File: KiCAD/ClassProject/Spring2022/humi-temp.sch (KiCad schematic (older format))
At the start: 2 parts

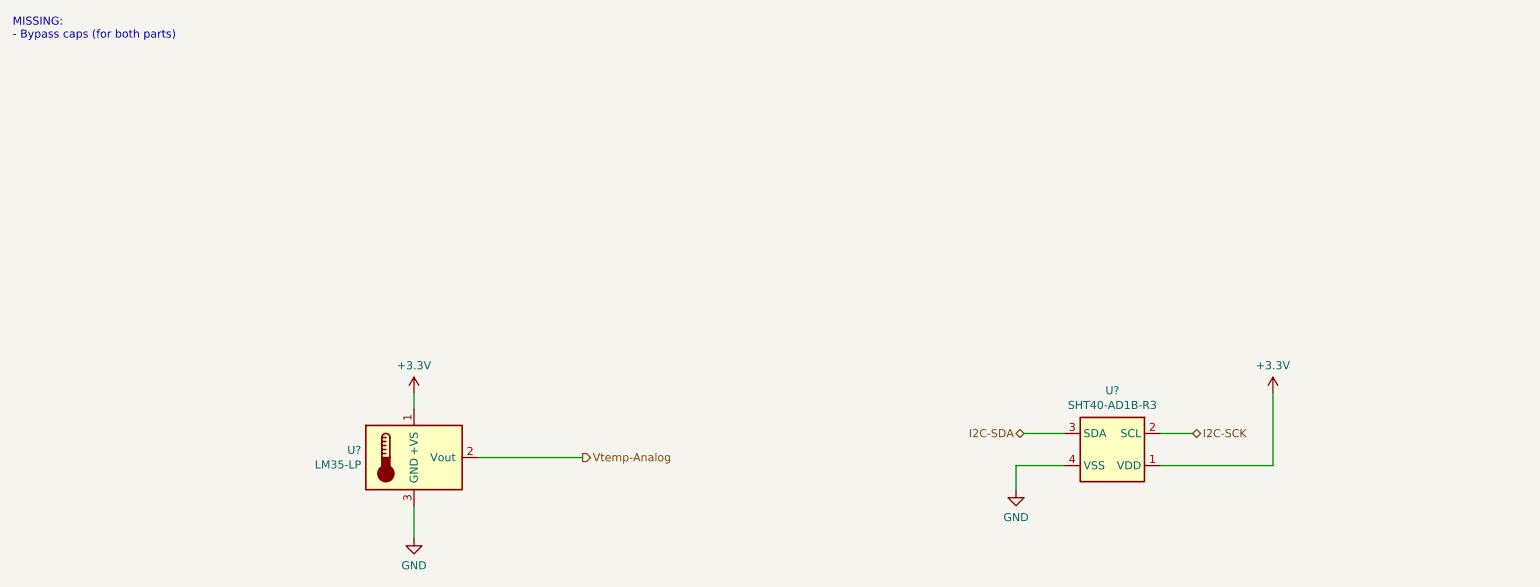
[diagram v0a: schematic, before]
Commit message: Added decoupling caps and pull up resistors from PONTECH library
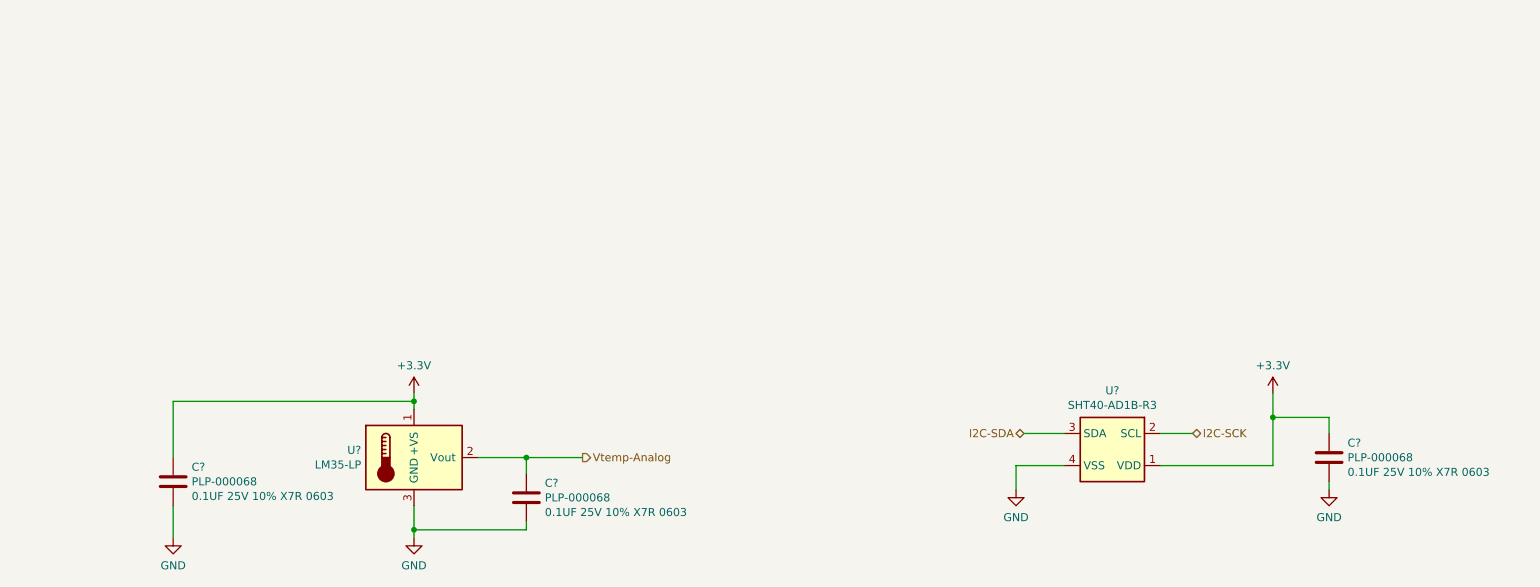
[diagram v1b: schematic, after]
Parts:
- added C? (x3): PLP-000068, a_pontech:CAP-NON-POLAR-0603, symbol 1_pontech:PLP-000068
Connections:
- net +3V3: now also C?.1, C?.1
- net GND: now also C?.2, C?.2, C?.2
- net Vtemp-Analog: now also C?.1
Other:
- note removed: "MISSING:\n- Bypass caps (for both parts)"
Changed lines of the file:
@@
 Comment4 ""
 $EndDescr
-Text Notes 950  1000 0    50   ~ 0
-MISSING:\n- Bypass caps (for both parts)
 $Comp
 L 74_Jacob:+3.3V #PWR?
@@
 $EndComp
 Wire Wire Line
-	8800 3200 8800 3650
+	8800 3200 8800 3350
 Wire Wire Line
 	8800 3650 8100 3650
@@
 $EndComp
 Wire Wire Line
-	3450 4100 3450 3900
+	3450 4100 3450 4050
 Text HLabel 4500 3600 2    50   Output ~ 0
 Vtemp-Analog
 Wire Wire Line
-	3850 3600 4500 3600
+	3850 3600 4150 3600
 $Comp
 L 74_Jacob:+3.3V #PWR?
@@
 	1    0    0    -1
 $EndComp
-Wire Wire Line
-	3450 3200 3450 3300
 Text HLabel 7250 3450 0    50   BiDi ~ 0
 I2C-SDA
@@
 Wire Wire Line
 	8300 3450 8100 3450
+$Comp
+L 1_pontech:PLP-000068 C?
+U 1 1 6264748D
+P 4150 3850
+F 0 "C?" H 4265 3941 50  0000 L CNN
+F 1 "PLP-000068" H 4265 3850 50  0000 L CNN
+F 2 "a_pontech:CAP-NON-POLAR-0603" H 4250 3400 50  0001 L CNN
+F 3 "~" H 4150 3850 50  0001 C CNN
+F 4 "0.1UF 25V 10% X7R 0603" H 4265 3759 50  0000 L CNN "Info"
+	1    4150 3850
+	1    0    0    -1
+$EndComp
+Connection ~ 4150 3600
+Wire Wire Line
+	4150 3600 4500 3600
+Wire Wire Line
+	4150 4050 3450 4050
+Connection ~ 3450 4050
+Wire Wire Line
+	4150 3700 4150 3600
+Wire Wire Line
+	4150 4000 4150 4050
+$Comp
+L 1_pontech:PLP-000068 C?
+U 1 1 626498A3
+P 1950 3750
+F 0 "C?" H 2065 3841 50  0000 L CNN
+F 1 "PLP-000068" H 2065 3750 50  0000 L CNN
+F 2 "a_pontech:CAP-NON-POLAR-0603" H 2050 3300 50  0001 L CNN
+F 3 "~" H 1950 3750 50  0001 C CNN
+F 4 "0.1UF 25V 10% X7R 0603" H 2065 3659 50  0000 L CNN "Info"
+	1    1950 3750
+	1    0    0    -1
+$EndComp
+Wire Wire Line
+	1950 3600 1950 3250
+$Comp
+L 74_Jacob:GND #PWR?
+U 1 1 6264A42D
+P 1950 4100
+F 0 "#PWR?" H 1950 3850 50  0001 C CNN
+F 1 "GND" H 1950 3927 50  0000 C CNN
+F 2 "" H 1950 4100 50  0001 C CNN
+F 3 "" H 1950 4100 50  0001 C CNN
+	1    1950 4100
+	1    0    0    -1
+$EndComp
+$Comp
+L 1_pontech:PLP-000068 C?
+U 1 1 6264AACE
+P 9150 3600
+F 0 "C?" H 9265 3691 50  0000 L CNN
+F 1 "PLP-000068" H 9265 3600 50  0000 L CNN
+F 2 "a_pontech:CAP-NON-POLAR-0603" H 9250 3150 50  0001 L CNN
+F 3 "~" H 9150 3600 50  0001 C CNN
+F 4 "0.1UF 25V 10% X7R 0603" H 9265 3509 50  0000 L CNN "Info"
+	1    9150 3600
+	1    0    0    -1
+$EndComp
+Wire Wire Line
+	9150 3450 9150 3350
+Wire Wire Line
+	9150 3350 8800 3350
+Connection ~ 8800 3350
+Wire Wire Line
+	8800 3350 8800 3650
+$Comp
+L 74_Jacob:GND #PWR?
+U 1 1 6264C084
+P 9150 3800
+F 0 "#PWR?" H 9150 3550 50  0001 C CNN
+F 1 "GND" H 9150 3627 50  0000 C CNN
+F 2 "" H 9150 3800 50  0001 C CNN
+F 3 "" H 9150 3800 50  0001 C CNN
+	1    9150 3800
+	1    0    0    -1
+$EndComp
+Wire Wire Line
+	9150 3750 9150 3800
+Wire Wire Line
+	1950 3900 1950 4100
+Wire Wire Line
+	3450 3900 3450 4050
+Wire Wire Line
+	3450 3250 3450 3300
+Wire Wire Line
+	3450 3200 3450 3250
+Connection ~ 3450 3250
+Wire Wire Line
+	1950 3250 3450 3250
 $EndSCHEMATC

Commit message: Added footprint for Mehdi's part.
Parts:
- U?: footprint (none) -> 74_mehdi:TO-92L_Inline
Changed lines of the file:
@@
 F 0 "U?" H 3121 3646 50  0000 R CNN
 F 1 "LM35-LP" H 3121 3555 50  0000 R CNN
-F 2 "" H 3500 3350 50  0001 L CNN
+F 2 "74_mehdi:TO-92L_Inline" H 3500 3350 50  0001 L CNN
 F 3 "" H 3450 3600 50  0001 C CNN
 	1    3450 3600

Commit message: Nearly finished schematic and routing.
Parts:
- gave numbers to parts that had none: 5
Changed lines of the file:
@@
 $EndDescr
 $Comp
-L 74_Jacob:+3.3V #PWR?
+L 74_Jacob:+3.3V #PWR0121
 U 1 1 6267B8DF
 P 8800 3200
-F 0 "#PWR?" H 8800 3050 50  0001 C CNN
+F 0 "#PWR0121" H 8800 3050 50  0001 C CNN
 F 1 "+3.3V" H 8800 3373 50  0000 C CNN
 F 2 "" H 8800 3200 50  0001 C CNN
@@
 $EndComp
 $Comp
-L 74_Mehdi_Library:LM35-LP U?
+L 74_Mehdi_Library:LM35-LP U10
 U 1 1 6267C272
 P 3450 3600
-F 0 "U?" H 3121 3646 50  0000 R CNN
+F 0 "U10" H 3121 3646 50  0000 R CNN
 F 1 "LM35-LP" H 3121 3555 50  0000 R CNN
 F 2 "74_mehdi:TO-92L_Inline" H 3500 3350 50  0001 L CNN
@@
 $EndComp
 $Comp
-L 74_eduardo_aaron:SHT40-AD1B-R3 U?
+L 74_eduardo_aaron:SHT40-AD1B-R3 U11
 U 1 1 6267D217
 P 7800 3550
-F 0 "U?" V 7433 3550 50  0000 C CNN
+F 0 "U11" V 7433 3550 50  0000 C CNN
 F 1 "SHT40-AD1B-R3" V 7524 3550 50  0000 C CNN
 F 2 "74_eduardo_aaron:SHTC1Humidity_temp_footprint" H 8000 3200 50  0001 C CNN
@@
 	8800 3650 8100 3650
 $Comp
-L 74_Jacob:GND #PWR?
+L 74_Jacob:GND #PWR0122
 U 1 1 6267E6D2
 P 7200 3800
-F 0 "#PWR?" H 7200 3550 50  0001 C CNN
+F 0 "#PWR0122" H 7200 3550 50  0001 C CNN
 F 1 "GND" H 7200 3627 50  0000 C CNN
 F 2 "" H 7200 3800 50  0001 C CNN
@@
 	7200 3650 7500 3650
 $Comp
-L 74_Jacob:GND #PWR?
+L 74_Jacob:GND #PWR0123
 U 1 1 6267EE1E
 P 3450 4100
-F 0 "#PWR?" H 3450 3850 50  0001 C CNN
+F 0 "#PWR0123" H 3450 3850 50  0001 C CNN
 F 1 "GND" H 3450 3927 50  0000 C CNN
 F 2 "" H 3450 4100 50  0001 C CNN
@@
 	3850 3600 4150 3600
 $Comp
-L 74_Jacob:+3.3V #PWR?
+L 74_Jacob:+3.3V #PWR0124
 U 1 1 6267F92C
 P 3450 3200
-F 0 "#PWR?" H 3450 3050 50  0001 C CNN
+F 0 "#PWR0124" H 3450 3050 50  0001 C CNN
 F 1 "+3.3V" H 3450 3373 50  0000 C CNN
 F 2 "" H 3450 3200 50  0001 C CNN
@@
 	8300 3450 8100 3450
 $Comp
-L 1_pontech:PLP-000068 C?
+L 1_pontech:PLP-000068 C2
 U 1 1 6264748D
 P 4150 3850
-F 0 "C?" H 4265 3941 50  0000 L CNN
+F 0 "C2" H 4265 3941 50  0000 L CNN
 F 1 "PLP-000068" H 4265 3850 50  0000 L CNN
 F 2 "a_pontech:CAP-NON-POLAR-0603" H 4250 3400 50  0001 L CNN
@@
 	4150 4000 4150 4050
 $Comp
-L 1_pontech:PLP-000068 C?
+L 1_pontech:PLP-000068 C1
 U 1 1 626498A3
 P 1950 3750
-F 0 "C?" H 2065 3841 50  0000 L CNN
+F 0 "C1" H 2065 3841 50  0000 L CNN
 F 1 "PLP-000068" H 2065 3750 50  0000 L CNN
 F 2 "a_pontech:CAP-NON-POLAR-0603" H 2050 3300 50  0001 L CNN
@@
 	1950 3600 1950 3250
 $Comp
-L 74_Jacob:GND #PWR?
+L 74_Jacob:GND #PWR0125
 U 1 1 6264A42D
 P 1950 4100
-F 0 "#PWR?" H 1950 3850 50  0001 C CNN
+F 0 "#PWR0125" H 1950 3850 50  0001 C CNN
 F 1 "GND" H 1950 3927 50  0000 C CNN
 F 2 "" H 1950 4100 50  0001 C CNN
@@
 $EndComp
 $Comp
-L 1_pontech:PLP-000068 C?
+L 1_pontech:PLP-000068 C3
 U 1 1 6264AACE
 P 9150 3600
-F 0 "C?" H 9265 3691 50  0000 L CNN
+F 0 "C3" H 9265 3691 50  0000 L CNN
 F 1 "PLP-000068" H 9265 3600 50  0000 L CNN
 F 2 "a_pontech:CAP-NON-POLAR-0603" H 9250 3150 50  0001 L CNN
@@
 	8800 3350 8800 3650
 $Comp
-L 74_Jacob:GND #PWR?
+L 74_Jacob:GND #PWR0126
 U 1 1 6264C084
 P 9150 3800
-F 0 "#PWR?" H 9150 3550 50  0001 C CNN
+F 0 "#PWR0126" H 9150 3550 50  0001 C CNN
 F 1 "GND" H 9150 3627 50  0000 C CNN
 F 2 "" H 9150 3800 50  0001 C CNN
